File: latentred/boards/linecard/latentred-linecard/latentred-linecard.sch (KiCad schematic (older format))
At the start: 7 parts, among them J1 CONN_LATENTRED_LINECARD_DEVICE

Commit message: Continued initial line card layout
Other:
- note added: "Swap some P/N pairs for easier routing\nCan correct FPGA-side or on backplane"
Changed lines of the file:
@@
 Sheet 1 3
 Title "LATENTRED 8-port 10/100/1000 Base-T Line Card"
-Date "2018-04-27"
+Date "2018-06-05"
 Rev "0.1"
 Comp "Andrew D. Zonenberg"
@@
 Text Notes 9050 2450 0    50   ~ 0
 TODO: Pulldown on PHY_RST_N
+Text Notes 5750 5150 0    50   ~ 0
+Swap some P/N pairs for easier routing\nCan correct FPGA-side or on backplane
 $EndSCHEMATC

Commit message: Updating file: latentred-linecard.kicad_pcb with current fully routed design
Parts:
- added R159: 1K, azonenberg_pcb:EIA_0402_RES_NOSILK, symbol device:R
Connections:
- net GND: now also R159.1
- net PHY_RST_N: now also R159.2
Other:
- note removed: "TODO: Pulldown on PHY_RST_N"
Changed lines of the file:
@@
 Text Notes 9050 2350 0    50   ~ 0
 TODO: Add reserved GPIO signal to connector\nTODO: Add reserved LVDS signal to connector
-Text Notes 9050 2450 0    50   ~ 0
-TODO: Pulldown on PHY_RST_N
 Text Notes 5750 5150 0    50   ~ 0
 Swap some P/N pairs for easier routing\nCan correct FPGA-side or on backplane
+$Comp
+L device:R R159
+U 1 1 62C8F62F
+P 1400 5800
+F 0 "R159" V 1350 6000 50  0000 C CNN
+F 1 "1K" V 1400 5800 50  0000 C CNN
+F 2 "azonenberg_pcb:EIA_0402_RES_NOSILK" V 1330 5800 50  0001 C CNN
+F 3 "" H 1400 5800 50  0001 C CNN
+	1    1400 5800
+	0    1    1    0
+$EndComp
+Text Label 1250 5800 2    50   ~ 0
+PHY_RST_N
+Text Label 1750 5800 0    50   ~ 0
+GND
+Wire Wire Line
+	1750 5800 1550 5800
 $EndSCHEMATC

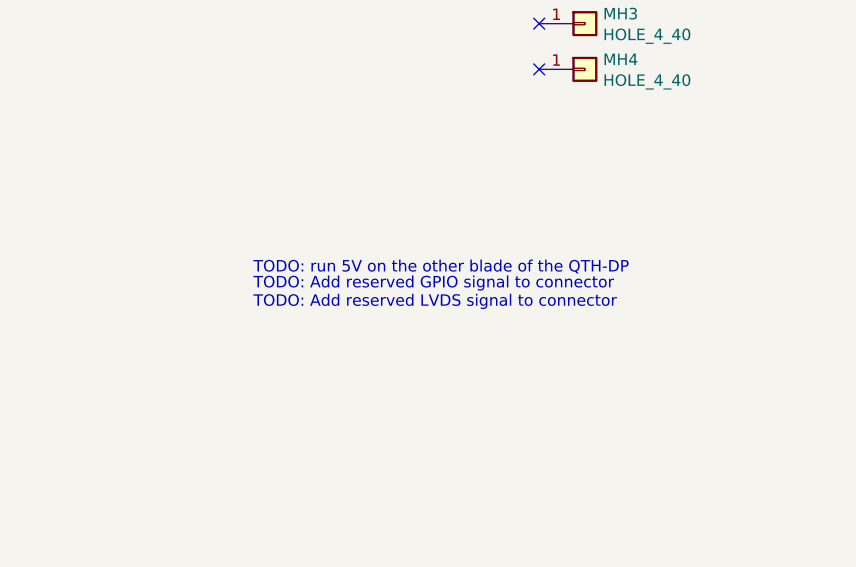
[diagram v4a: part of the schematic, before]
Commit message: Line card: updates to text descriptions at top level
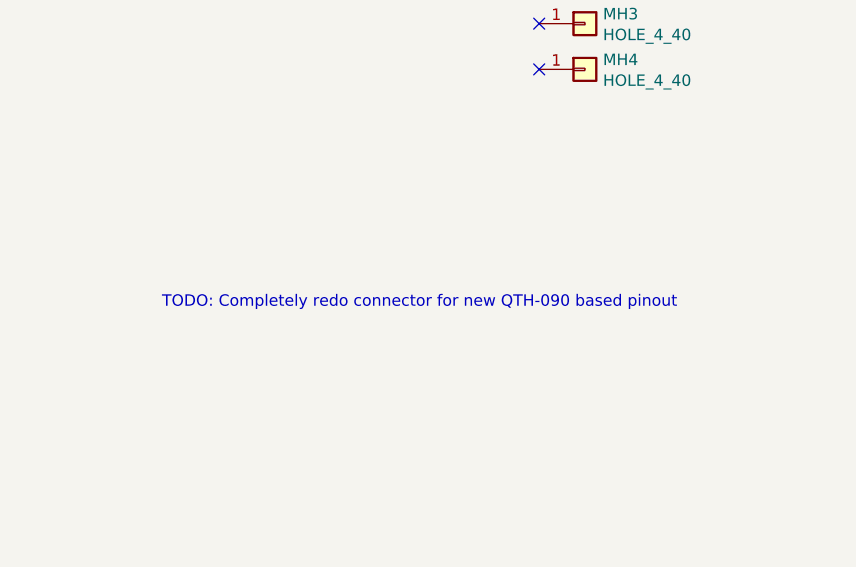
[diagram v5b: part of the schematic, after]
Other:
- note added: "TODO: Completely redo connector for new QTH-090 based pinout"
- note removed: "TODO: Add reserved GPIO signal to connector\nTODO: Add reserved LVDS signal to connector"
- note removed: "TODO: run 5V on the other blade of the QTH-DP"
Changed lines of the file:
@@
 EESchema Schematic File Version 4
 LIBS:latentred-linecard-cache
-EELAYER 26 0
+EELAYER 30 0
 EELAYER END
 $Descr A4 11693 8268
@@
 Sheet 1 3
 Title "LATENTRED 8-port 10/100/1000 Base-T Line Card"
-Date "2018-06-05"
+Date "2019-09-09"
 Rev "0.1"
 Comp "Andrew D. Zonenberg"
@@
 $EndComp
 NoConn ~ 10300 1300
-Text Notes 9050 2200 0    50   ~ 0
-TODO: run 5V on the other blade of the QTH-DP
-Text Notes 9050 2350 0    50   ~ 0
-TODO: Add reserved GPIO signal to connector\nTODO: Add reserved LVDS signal to connector
 Text Notes 5750 5150 0    50   ~ 0
 Swap some P/N pairs for easier routing\nCan correct FPGA-side or on backplane
@@
 Wire Wire Line
 	1750 5800 1550 5800
+Text Notes 8650 2350 0    50   ~ 0
+TODO: Completely redo connector for new QTH-090 based pinout
 $EndSCHEMATC
